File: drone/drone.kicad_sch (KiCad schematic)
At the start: 44 parts, among them J1 UART, J2 HMC5883, J3 Conn_01x04_Socket, J4 Conn_01x04_Socket, J5 Conn_01x04_Socket, J6 Conn_01x04_Socket, SW1 SW_Push, SW2 SW_Push, U1 ESP32-WROOM-32D, U2 MPU-6050, U3 MP2303ADN

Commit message: tiep tuc dj + gitignore
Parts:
- removed J1: UART, Connector_PinHeader_2.54mm:PinHeader_1x04_P2.54mm_Vertical, symbol Connector:Conn_01x04_Pin
- removed J3, J4, J5, J6: Conn_01x04_Socket, Connector_JST:JST_GH_SM04B-GHS-TB_1x04-1MP_P1.25mm_Horizontal, symbol Connector:Conn_01x04_Socket
- removed R12, R13, R14, R15, R5, R6: 4.7k, Resistor_SMD:R_0805_2012Metric_Pad1.20x1.40mm_HandSolder, symbol Device:R
- added C13: 0.1uF, Capacitor_SMD:C_0805_2012Metric_Pad1.18x1.45mm_HandSolder, symbol Device:C
- added J3: Conn_01x03_Pin, Connector_PinHeader_2.54mm:PinHeader_1x03_P2.54mm_Vertical, symbol Connector:Conn_01x03_Pin
- added TP10, TP3, TP4, TP5, TP6, TP7, TP8, TP9: TestPoint, TestPoint:TestPoint_Pad_D2.5mm, symbol Connector:TestPoint
- added TP11, TP12, TP13, TP14, TP15, TP16, TP17, TP18: TestPoint, TestPoint:TestPoint_Pad_1.5x1.5mm, symbol Connector:TestPoint
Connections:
- net VCC is gone; now on net ESC VCC: R2.2, R8.2, TP1.1, U3.2 (IN)
- net Batt Read: now also C13.1
- net ESC VCC: now also TP10.1, TP4.1, TP6.1, TP8.1
- net ESC1: now also U1.13 (IO14), TP12.1; no longer U1.23 (IO15)
- net ESC2: now also U1.14 (IO12), TP14.1; no longer U1.27 (IO16)
- net ESC3: now also TP16.1
- net ESC4: now also TP18.1
- net GND: now also C13.2, J3.1 (Pin_1)
- net RX: now also J3.3 (Pin_3)
- net TX: now also J3.2 (Pin_2)
- new net ESC GND: TP3.1, TP5.1, TP7.1, TP9.1

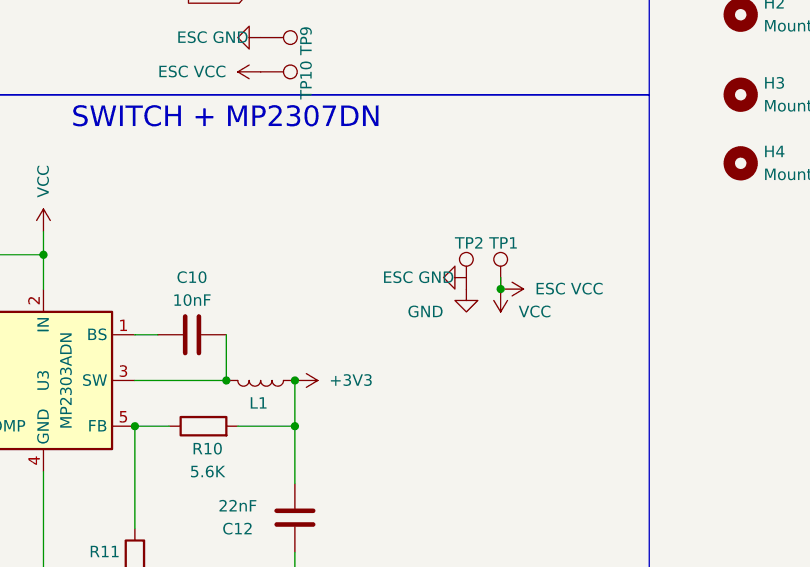
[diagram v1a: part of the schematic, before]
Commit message: esc wired
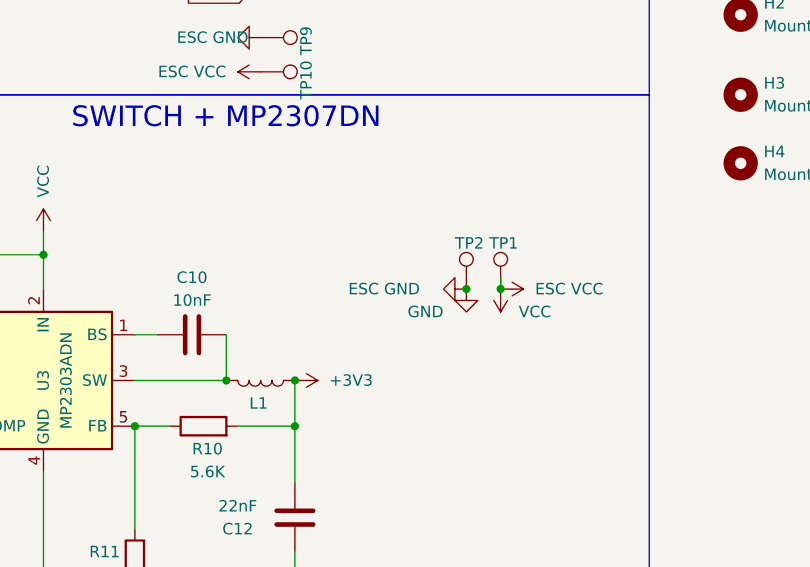
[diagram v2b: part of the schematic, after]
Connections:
- net GND is gone; now on net ESC GND: C1.1, C12.2, C13.2, C2.1, C3.2, C5.2, C6.2, C7.1, C8.1, C9.2, J2.2 (Pin_2), J3.1 (Pin_1), R11.2, R7.1, R9.2, SW1.1, SW2.2, TP2.1, U1.1 (GND), U1.15 (GND), U1.38 (GND), U1.39_1 (GND), U1.39_10 (GND), U1.39_11 (GND), U1.39_12 (GND), U1.39_13 (GND), U1.39_14 (GND), U1.39_15 (GND), U1.39_16 (GND), U1.39_17 (GND), U1.39_18 (GND), U1.39_19 (GND), U1.39_2 (GND), U1.39_20 (GND), U1.39_21 (GND), U1.39_3 (GND), U1.39_4 (GND), U1.39_5 (GND), U1.39_6 (GND), U1.39_7 (GND), U1.39_8 (GND), U1.39_9 (GND), U2.1 (CLKIN), U2.11 (FSYNC), U2.14 (NC), U2.15 (NC), U2.16 (NC), U2.17 (NC), U2.18 (GND), U2.2 (NC), U2.3 (NC), U2.4 (NC), U2.5 (NC), U3.4 (GND)
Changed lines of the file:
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@@
+	)
+	(junction
+		(at 156.21 157.48)
+		(diameter 0)
+		(color 0 0 0 0)
 	)
 	(junction
@@
 	(symbol
 		(lib_id "power:GND")
-		(at 156.21 156.21 270)
+		(at 156.21 157.48 270)
 		(unit 1)
 		(body_style 1)
@@
 		(dnp no)
 		(property "Reference" "#PWR042"
-			(at 149.86 156.21 0)
+			(at 149.86 157.48 0)
 			(hide yes)
 			(show_name no)
@@
 		)
 		(property "Value" "ESC GND"
-			(at 150.876 156.21 90)
+			(at 147.066 157.48 90)
 			(show_name no)
 			(do_not_autoplace no)
@@
 		)
 		(property "Footprint" ""
-			(at 156.21 156.21 0)
+			(at 156.21 157.48 0)
 			(hide yes)
 			(show_name no)
@@
 		)
 		(property "Datasheet" ""
-			(at 156.21 156.21 0)
+			(at 156.21 157.48 0)
 			(hide yes)
 			(show_name no)
@@
 		)
 		(property "Description" "Power symbol creates a global label with name \"GND\" , ground"
-			(at 156.21 156.21 0)
-			(hide yes)
-			(show_name no)
+			(at 156.21 157.48 0)
+			(hide yes)
+			(show_name no)

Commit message: copper pour 16/4
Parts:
- added NT1: NetTie_2, NetTie:NetTie-2_SMD_Pad2.0mm, symbol Device:NetTie_2
- SW1, SW2: footprint Button_Switch_THT:SW_PUSH_6mm_H4.3mm -> Button_Switch_SMD:SW_SPST_TS-1088-xR025
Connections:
- net ESC GND: now also NT1.1; no longer C1.1, C12.2, C13.2, C2.1, C3.2, C5.2, C6.2, C7.1, C8.1, C9.2, J2.2 (Pin_2), J3.1 (Pin_1), R11.2, R7.1, R9.2, SW1.1, SW2.2, TP2.1, U1.1 (GND), U1.15 (GND), U1.38 (GND), U1.39_1 (GND), U1.39_10 (GND), U1.39_11 (GND), U1.39_12 (GND), U1.39_13 (GND), U1.39_14 (GND), U1.39_15 (GND), U1.39_16 (GND), U1.39_17 (GND), U1.39_18 (GND), U1.39_19 (GND), U1.39_2 (GND), U1.39_20 (GND), U1.39_21 (GND), U1.39_3 (GND), U1.39_4 (GND), U1.39_5 (GND), U1.39_6 (GND), U1.39_7 (GND), U1.39_8 (GND), U1.39_9 (GND), U2.1 (CLKIN), U2.11 (FSYNC), U2.14 (NC), U2.15 (NC), U2.16 (NC), U2.17 (NC), U2.18 (GND), U2.2 (NC), U2.3 (NC), U2.4 (NC), U2.5 (NC), U3.4 (GND)
- new net GND: C1.1, C12.2, C13.2, C2.1, C3.2, C5.2, C6.2, C7.1, C8.1, C9.2, J2.2 (Pin_2), J3.1 (Pin_1), NT1.2, R11.2, R7.1, R9.2, SW1.1, SW2.2, TP2.1, U1.1 (GND), U1.15 (GND), U1.38 (GND), U1.39_1 (GND), U1.39_10 (GND), U1.39_11 (GND), U1.39_12 (GND), U1.39_13 (GND), U1.39_14 (GND), U1.39_15 (GND), U1.39_16 (GND), U1.39_17 (GND), U1.39_18 (GND), U1.39_19 (GND), U1.39_2 (GND), U1.39_20 (GND), U1.39_21 (GND), U1.39_3 (GND), U1.39_4 (GND), U1.39_5 (GND), U1.39_6 (GND), U1.39_7 (GND), U1.39_8 (GND), U1.39_9 (GND), U2.1 (CLKIN), U2.11 (FSYNC), U2.14 (NC), U2.15 (NC), U2.16 (NC), U2.17 (NC), U2.18 (GND), U2.2 (NC), U2.3 (NC), U2.4 (NC), U2.5 (NC), U3.4 (GND)
